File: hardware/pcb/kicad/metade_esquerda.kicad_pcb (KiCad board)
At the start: 2 copper layers, 125.4 x 105.5 mm, 177 parts

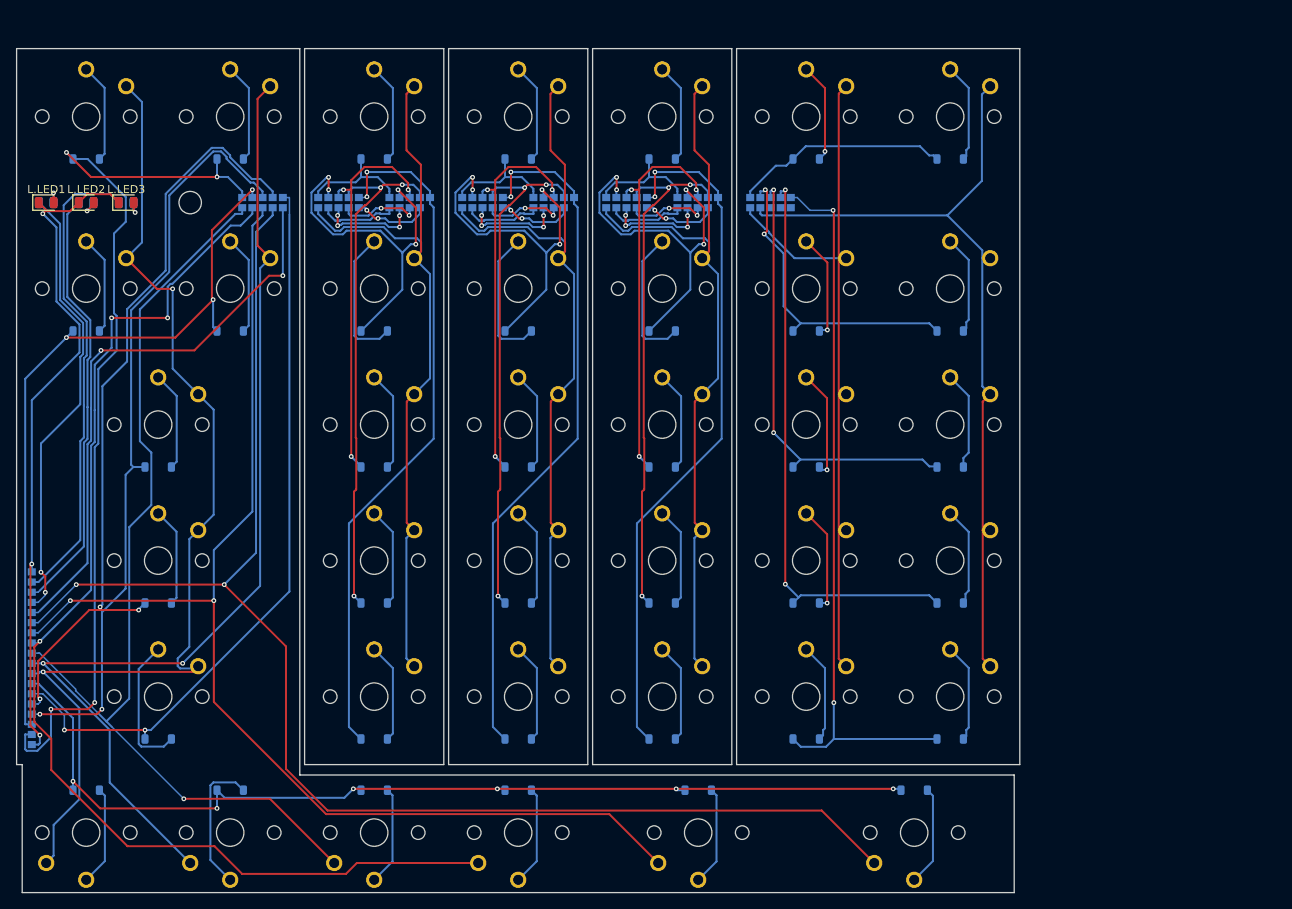
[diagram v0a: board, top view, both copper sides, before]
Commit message: Metade esquerda: placas afastadas 8 mm para ver onde cada uma acaba
Co-Authored-By: Claude Opus 5.5 <noreply@anthropic.com>
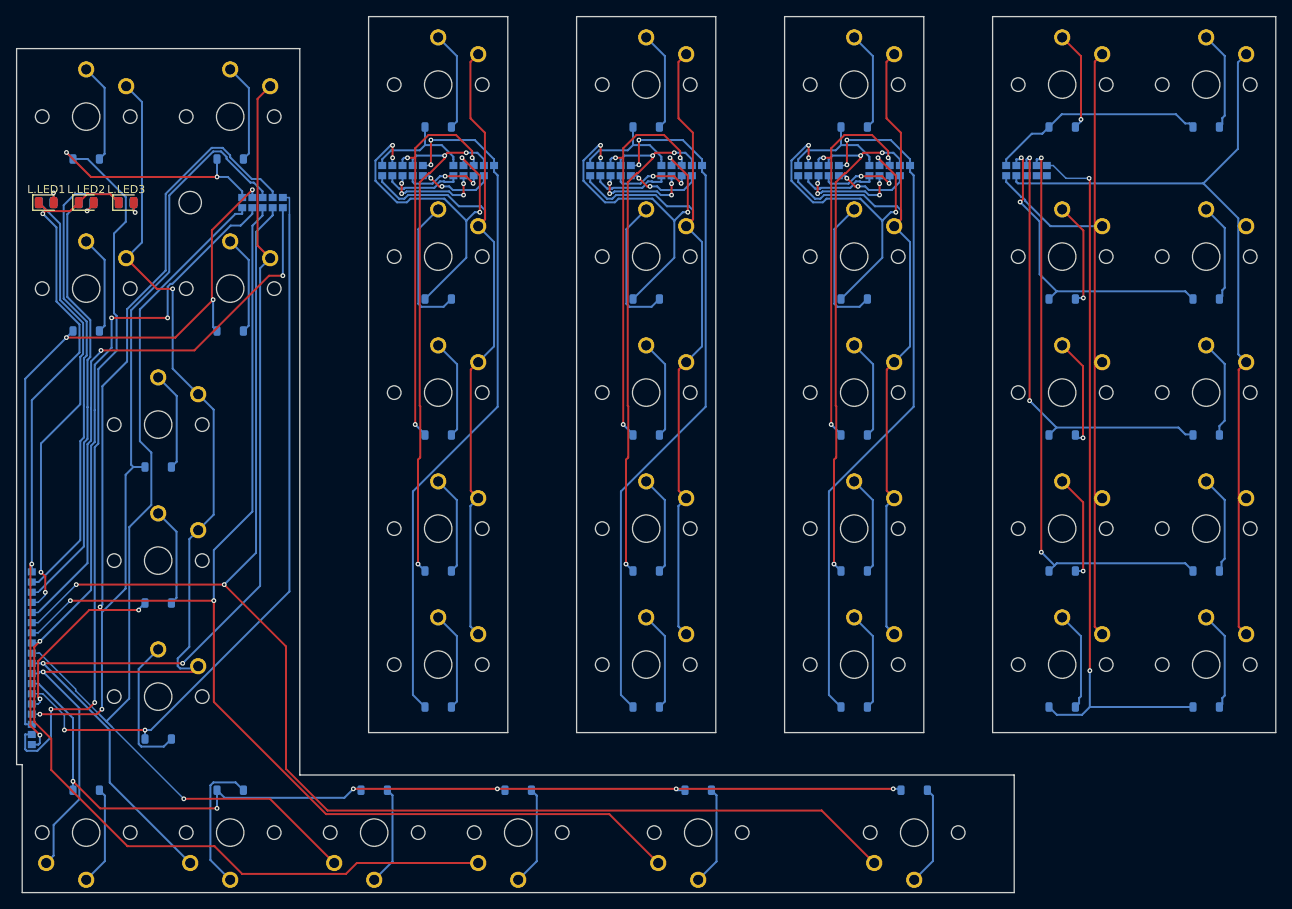
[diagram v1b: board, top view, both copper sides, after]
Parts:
- moved IN.PAD3 32.2 mm to (273.5, 109.6)
- moved IN.PAD8 32.2 mm to (273.5, 110.9)
- moved IN.D1 32.2 mm to (278.0, 177.3)
- moved IN.D10 32.2 mm to (296.0, 104.8)
- moved IN.D2 32.2 mm to (278.0, 160.3)
- moved IN.D3 32.2 mm to (278.0, 143.3)
- moved IN.D4 32.2 mm to (278.0, 126.3)
- moved IN.D5 32.2 mm to (278.0, 104.8)
- moved IN.D6 32.2 mm to (296.0, 177.3)
- moved IN.D7 32.2 mm to (296.0, 160.3)
- moved IN.D8 32.2 mm to (296.0, 143.3)
- moved IN.D9 32.2 mm to (296.0, 126.3)
- moved IN.PAD1 32.2 mm to (271.0, 109.6)
- moved IN.PAD4 32.2 mm to (274.8, 109.6)
- moved IN.PAD6 32.2 mm to (271.0, 110.9)
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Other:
- board size 125.4 x 105.5 mm -> 157.4 x 109.5 mm
